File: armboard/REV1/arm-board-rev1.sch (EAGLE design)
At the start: 36 parts, among them J2_12V ANDERSON_POWERPOLEPP45_PCB_HO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, J2_GND ANDERSON_POWERPOLEPP45_PCB_HO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

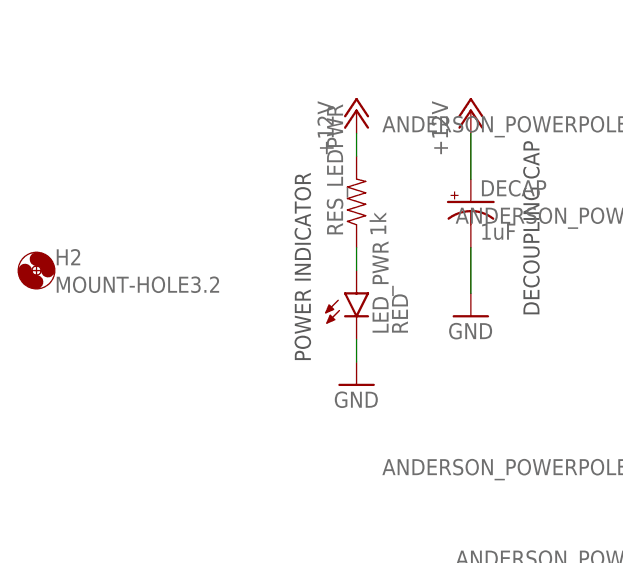
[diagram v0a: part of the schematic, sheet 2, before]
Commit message: moved around and organized in folders, added sdc2130 moco profile, added arm-board-rev1-bom
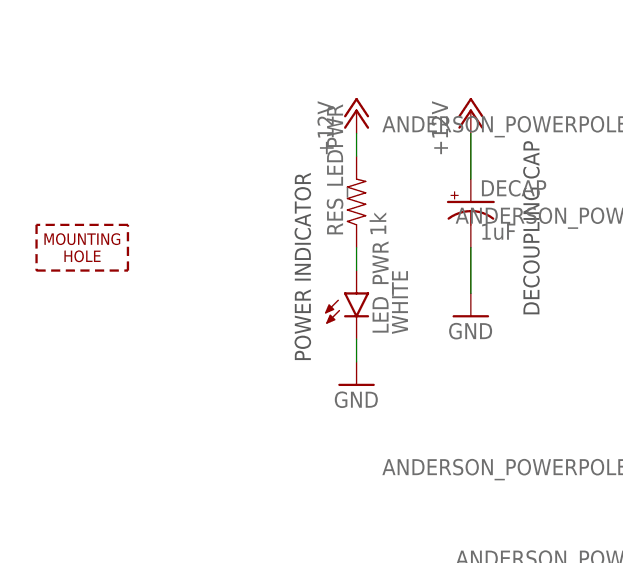
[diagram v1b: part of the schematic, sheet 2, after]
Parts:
- H2: value MOUNT-HOLE3.2 -> MOUNTING_HOLEM6; device holes:MOUNT-HOLE3.2 -> MRDT-Hardware:MOUNTING_HOLEM6
- LED_DYNASWD: value RED -> ORANGE
- LED_PWR: value RED -> WHITE
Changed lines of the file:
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@@
 <part name="GND6" library="SparkFun-Aesthetics" deviceset="GND" device=""/>
 <part name="RES_LEDDYNASWD" library="SparkFun-Resistors" deviceset="RESISTOR" device="1206" value="470"/>
-<part name="LED_DYNASWD" library="SparkFun-LED" deviceset="LED" device="1206" value="RED"/>
+<part name="LED_DYNASWD" library="SparkFun-LED" deviceset="LED" device="1206" value="ORANGE"/>
 <part name="RES_LEDPWR" library="SparkFun-Passives" deviceset="RESISTOR" device="1206" value="1k"/>
-<part name="LED_PWR" library="SparkFun-LED" deviceset="LED" device="1206" value="RED"/>
+<part name="LED_PWR" library="SparkFun-LED" deviceset="LED" device="1206" value="WHITE"/>
 <part name="GND2" library="SparkFun" deviceset="GND" device=""/>
 <part name="GND8" library="SparkFun-Aesthetics" deviceset="GND" device=""/>
@@
 <part name="ENC_EI" library="con-molex" deviceset="53?-03" device="261" value="53261-03"/>
 <part name="DECAP" library="SparkFun-Capacitors" deviceset="100UF-25V-20%(PTH)" device="" value="1uF"/>
-<part name="H2" library="holes" deviceset="MOUNT-HOLE" device="3.2"/>
+<part name="H2" library="MRDT-Hardware" deviceset="MOUNTING_HOLE" device="M6" value="MOUNTING_HOLEM6"/>
 <part name="GND7" library="SparkFun-Aesthetics" deviceset="GND" device=""/>
 <part name="P+10" library="supply1" deviceset="+12V" device=""/>
@@
 </schematic>
 </drawing>
+<compatibility>
+<note version="6.3" minversion="6.2.2" severity="warning">
+Since Version 6.2.2 text objects can contain more than one line,
+which will not be processed correctly with this version.
+</note>
+</compatibility>
 </eagle>
